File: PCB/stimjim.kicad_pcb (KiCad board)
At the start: 4 copper layers, 129 x 79.5 mm, 193 parts, among them J1 Conn_02x08_Odd_Even, J10 USB4105-GF-A, J11 BM03B-SRSS-TB, J2 Conn_Coaxial, J3 Conn_Coaxial, J4 10129383-910002ALF, J6 Screw_Terminal_01x02, J7 Conn_Coaxial, J8 Screw_Terminal_01x02, J9 Conn_Coaxial, SW2 PTS645VH58-2 LFS, SW3 TS04-66-50-BK-160-SMT, U10 AMP03, U11 INA826, U12 DG509ACWE, U13 CC3-0512DF-E, U14 ISO7760, U15 ISO7741, U151 AP2112K-3.3, U16 L78L05_SO8, U17 AD5752, U18 AD7321, U19 AD1582, U2 CC3-0512DF-E, U20 OPA197, U21 AMP03, U22 INA826, U23 DG509ACWE, U24 RP2354B, U25 W25Q128JVS, U3 ISO7760, U4 ISO7741, U5 L78L05_SO8, U6 AD5752, U7 AD7321, U8 AD1582, U9 OPA197, Y1 ABM8AIG-12.000MHZ-12-2Z-T3

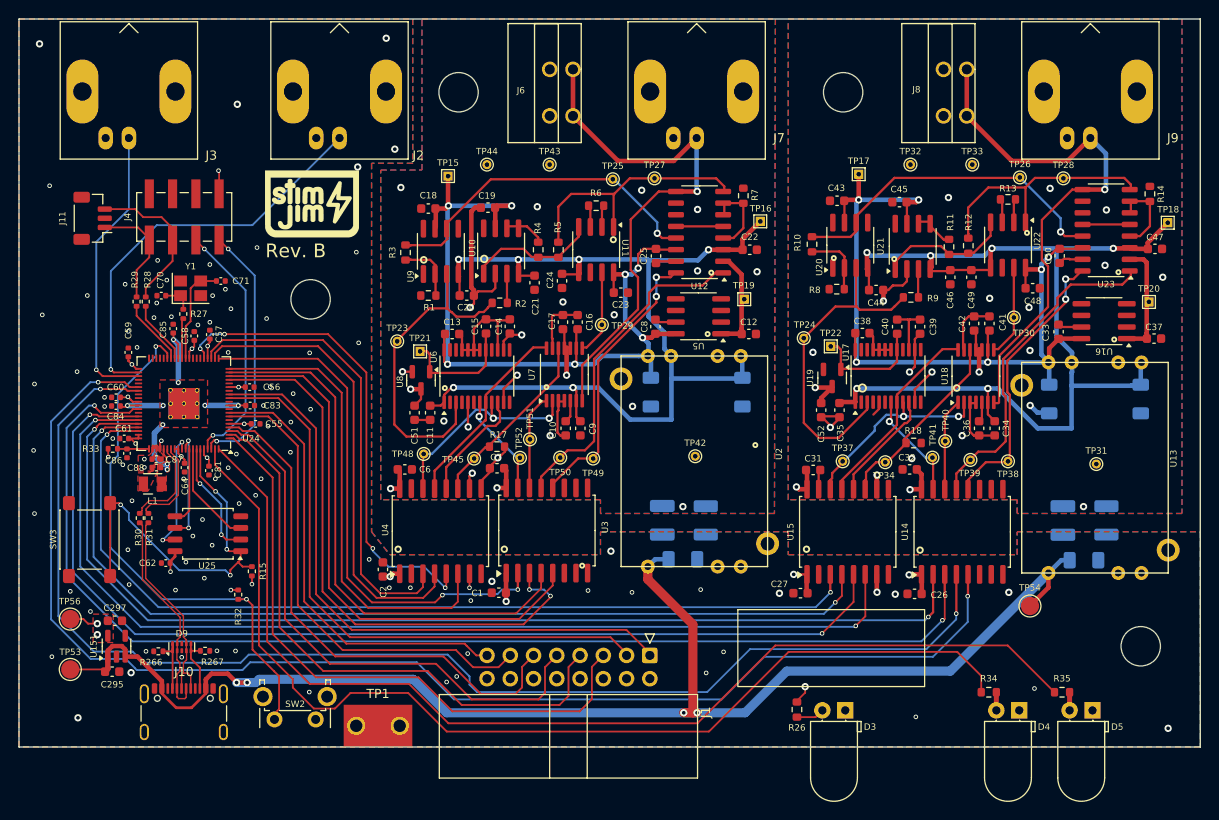
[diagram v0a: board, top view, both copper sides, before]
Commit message: Stimjim Rev. B candidate
- Sent to fab
- Lots of manufacturability changes
- BOM consolidation
- Repo layout changed a bit to remove redundant information. e.g.
  datasheet links are embedded in schematic. BOM information embedded in
  schematic. etc
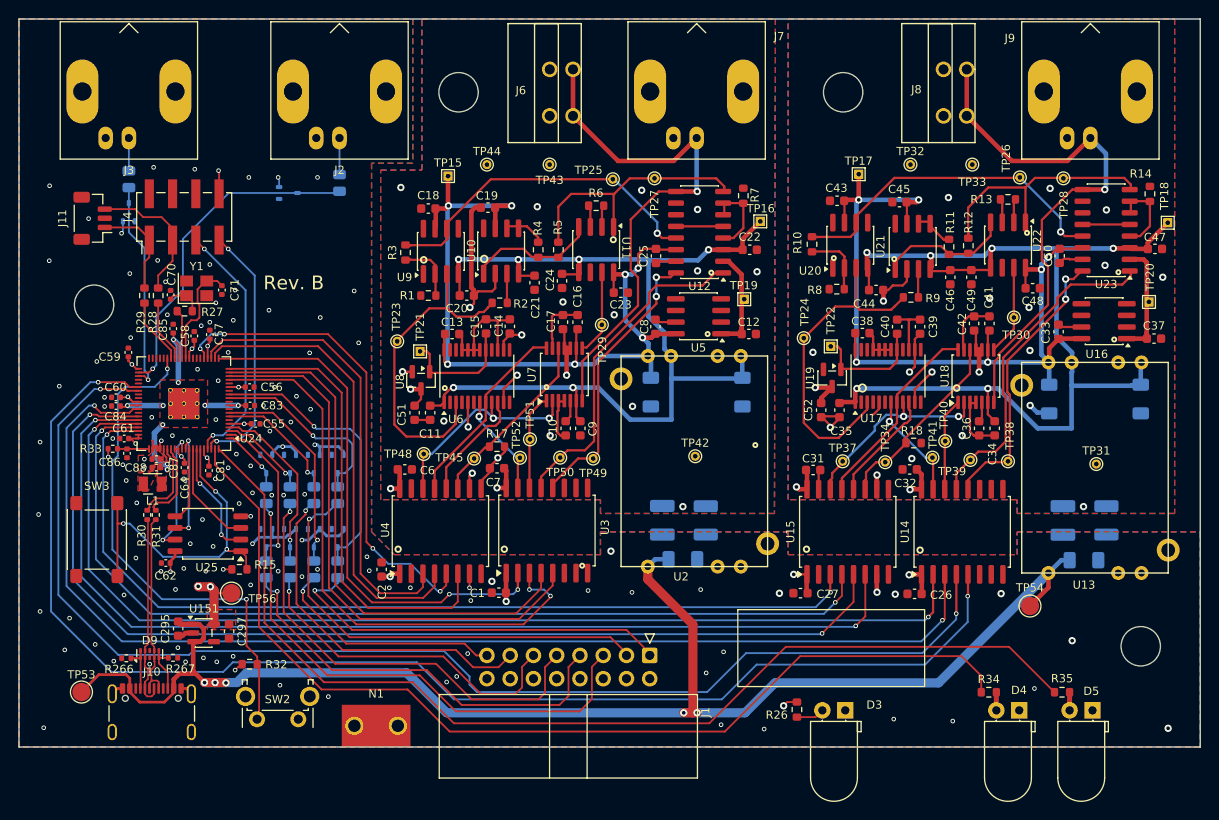
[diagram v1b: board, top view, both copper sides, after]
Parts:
- removed the G*** at (179.1, 108.4)
- removed the G*** at (178.9, 108.4)
- added D1: BAT54SW, Package_TO_SOT_SMD:SOT-323_SC-70, B.Cu at (176.4, 107.5)
- added D10: BAT54SW, Package_TO_SOT_SMD:SOT-323_SC-70, B.Cu at (179.2, 137.1)
- added D11: BAT54SW, Package_TO_SOT_SMD:SOT-323_SC-70, B.Cu at (176.6, 145.2)
- added D12: BAT54SW, Package_TO_SOT_SMD:SOT-323_SC-70, B.Cu at (176.6, 137.1)
- added D13: BAT54SW, Package_TO_SOT_SMD:SOT-323_SC-70, B.Cu at (174.0, 145.2)
- added D14: BAT54SW, Package_TO_SOT_SMD:SOT-323_SC-70, B.Cu at (174.0, 137.1)
- added D15: BAT54SW, Package_TO_SOT_SMD:SOT-323_SC-70, B.Cu at (181.8, 137.1)
- added D16: BAT54SW, Package_TO_SOT_SMD:SOT-323_SC-70, B.Cu at (181.8, 145.2)
- added D6: BAT54SW, Package_TO_SOT_SMD:SOT-323_SC-70, B.Cu at (159.0, 109.6)
- added D8: BAT54SW, Package_TO_SOT_SMD:SOT-323_SC-70, B.Cu at (179.2, 145.2)
- added G***: LOGO, LOGO, F.Cu at (178.2, 110.9)
- added R16: 270, Resistor_SMD:R_0805_2012Metric, B.Cu at (159.0, 106.0)
- added R21: 270, Resistor_SMD:R_0805_2012Metric, B.Cu at (179.2, 148.6)
- added R22: 270, Resistor_SMD:R_0805_2012Metric, B.Cu at (179.2, 140.5)
- added R23: 270, Resistor_SMD:R_0805_2012Metric, B.Cu at (176.6, 148.6)
- added R24: 270, Resistor_SMD:R_0805_2012Metric, B.Cu at (176.6, 140.5)
- added R25: 270, Resistor_SMD:R_0805_2012Metric, B.Cu at (174.0, 148.6)
- added R36: 270, Resistor_SMD:R_0805_2012Metric, B.Cu at (174.0, 140.5)
- added R37: 270, Resistor_SMD:R_0805_2012Metric, B.Cu at (181.8, 140.5)
- added R38: 270, Resistor_SMD:R_0805_2012Metric, B.Cu at (181.8, 148.6)
- added R39: 270, Resistor_SMD:R_0805_2012Metric, B.Cu at (182.0, 106.4)
- J1: value Conn_02x08_Odd_Even -> 302-R161
- J2, J3, J7, J9: value Conn_Coaxial -> 0731375003
- J6, J8: value Screw_Terminal_01x02 -> 1-2834016-2
- N1: renamed from TP1; value TestPoint -> SMTRA_M3-7-5ET
- R15, R27, R28, R29, R32: footprint Resistor_SMD:R_0402_1005Metric -> Resistor_SMD:R_0603_1608Metric
- R19, R20: value 1M -> 2.2M
- R33: value 33 -> 27
- U12, U23: value DG509ACWE -> DG409DYZ-T
- U16, U5: value L78L05_SO8 -> MC78L05ACDR2G
- moved H3 23.6 mm to (155.2, 119.7)
- moved TP56 17.8 mm to (170.2, 151.2), turned to 0 degrees
- moved C297 12.5 mm to (169.9, 155.4), turned to -90 degrees
- moved U151 9.62 mm to (167.2, 155.5), turned to 0 degrees
- moved C295 8.60 mm to (164.4, 155.1), turned to -90 degrees
- moved R32 7.70 mm to (172.2, 159.0), turned to 0 degrees
- moved D9 3.58 mm to (161.3, 157.9)
- moved R266 3.58 mm to (158.7, 158.3)
- moved R267 3.58 mm to (163.8, 158.3)
- moved J10 3.50 mm to (161.5, 165.3)
- moved TP53 2.75 mm to (153.8, 162.0)
- moved SW2 1.90 mm to (177.5, 165.0)
- moved R28 1.51 mm to (162.2, 118.7)
- moved R15 1.38 mm to (171.1, 148.6), turned to 0 degrees
- moved R29 1.08 mm to (160.7, 118.7)
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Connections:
- J1 pad 1: /GPIO0 -> /MCU/GPIO7_{P}
- J1 pad 11: /GPIO5 -> /MCU/GPIO2_{P}
- J1 pad 13: /GPIO6 -> /MCU/GPIO1_{P}
- J1 pad 15: /GPIO7 -> /MCU/GPIO0_{P}
- J1 pad 3: /GPIO1 -> /MCU/GPIO6_{P}
- J1 pad 5: /GPIO2 -> /MCU/GPIO5_{P}
- J1 pad 7: /GPIO3 -> /MCU/GPIO4_{P}
- J1 pad 9: /GPIO4 -> /MCU/GPIO3_{P}
- U24 pad 1: /GPIO2 -> /MCU/GPIO5
- U24 pad 12: /GPIO1 -> /MCU/GPIO6
- U24 pad 13: /GPIO0 -> /MCU/GPIO7
- U24 pad 2: /GPIO3 -> /MCU/GPIO4
- U24 pad 3: /GPIO4 -> /MCU/GPIO3
- U24 pad 4: /GPIO5 -> /MCU/GPIO2
- U24 pad 42: Net-(J2-In) -> /MCU/TRIG0
- U24 pad 43: Net-(J3-In) -> /MCU/TRIG1
- U24 pad 7: /GPIO6 -> /MCU/GPIO1
- U24 pad 8: /GPIO7 -> /MCU/GPIO0
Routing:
- net /GPIO0: track 68.3 -> 0.00 mm
- net /GPIO2: track 67.8 -> 0.00 mm
- net /GPIO1: track 65.7 -> 0.00 mm
- net /GPIO3: track 64.5 -> 0.00 mm
- net /GPIO4: track 61.0 -> 0.00 mm
- net /GPIO5: track 57.6 -> 0.00 mm
- net /MCU/GPIO5_{P}: track 0.00 -> 57.3 mm, vias 0 -> 1
- net /GPIO6: track 52.8 -> 0.00 mm
- net /MCU/GPIO6_{P}: track 0.00 -> 49.6 mm, vias 0 -> 1
- net /MCU/GPIO3_{P}: track 0.00 -> 49.6 mm, vias 0 -> 1
- net /GPIO7: track 49.2 -> 0.00 mm
- net /MCU/GPIO4_{P}: track 0.00 -> 46.2 mm, vias 0 -> 1
- net /MCU/GPIO7_{P}: track 0.00 -> 43.0 mm, vias 0 -> 1
- net Net-(J2-In): track 44.9 -> 3.99 mm, vias 1 -> 0
- net /MCU/GPIO1_{P}: track 0.00 -> 38.6 mm, vias 0 -> 1
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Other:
- board text added: "(e.g. JLC04161H-7628)"
- board text added: "0"
- board text added: "0 mm"
- board text added: "0.01 mm"
- board text added: "0.0152 mm"
- board text added: "0.02"
- board text added: "0.035 mm"
- board text added: "0.2104 mm"
- board text added: "1"
- board text added: "1.065 mm"
- board text added: "3.3"
- board text added: "4.5"
- board text added: "B.Cu"
- board text added: "B.Mask"
- board text added: "B.Paste"
- board text added: "B.Silkscreen"
- board text added: "Bottom Silk Screen"
- board text added: "Bottom Solder Mask"
- board text added: "Bottom Solder Paste"
- board text added: "Color"
- board text added: "Dielectric 1"
- board text added: "Dielectric 2"
- board text added: "Dielectric 3"
- board text added: "Epsilon R"
- board text added: "F.Cu"
- board text added: "F.Mask"
- board text added: "F.Paste"
- board text added: "F.Silkscreen"
- board text added: "FR4"
- board text added: "In1.Cu"
- board text added: "In2.Cu"
- board text added: "Layer Name"
- board text added: "Loss Tangent"
- board text added: "Material"
- board text added: "Not specified"
- board text added: "Thickness (mm)"
- board text added: "Top Silk Screen"
- board text added: "Top Solder Mask"
- board text added: "Top Solder Paste"
- board text added: "Type"
- board text added: "copper"
- board text added: "core"
- board text added: "prepreg"

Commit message: Rev C First Draft
- Fix and move LED footprints
- Move bar code sticker
- Add op-amp unity voltage follower to ADC input
- Remove screw terminals
- Made panel screw holes bigger both panels (3.2mm -> 3.7mm) for 3.4mm
  screws
- Create cutout for mounting rail on panels
- Delete the file with both back and front panels
- Update all footprints (except rp2354b so that its thermal vias pass DRC)
- Add component class and custom rule for USB-C footprint
- Indicate M3 screw in schematic + Add to BOM
- Improve adherence to ADC/DAC datasheets:
  - Move high speed signals out from under ADC (put MISO in +5V layer under ADC)
  - Add 10uF decoupling caps to ADC/DAC
- Change enclosure part number to black enclosure
- Add some more GND vias to isolated GND planes
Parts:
- removed J6, J8: 1-2834016-2, microstim:1-2834016-2 _TERM_BLK_2P_SIDE_ENT_2.54MM_PCB
- added C63: 0.1uF, Capacitor_SMD:C_0603_1608Metric, F.Cu at (244.8, 100.9)
- added C65: 0.1uF, Capacitor_SMD:C_0603_1608Metric, F.Cu at (201.8, 101.8)
- added C66: 0.1uF, Capacitor_SMD:C_0603_1608Metric, F.Cu at (254.5, 97.6)
- added C67: 0.1uF, Capacitor_SMD:C_0603_1608Metric, F.Cu at (211.5, 98.6)
- added C68: 10uF, Capacitor_SMD:C_0603_1608Metric, F.Cu at (239.1, 121.3)
- added C69: 10uF, Capacitor_SMD:C_0603_1608Metric, F.Cu at (192.1, 122.2)
- added C72: 10uF, Capacitor_SMD:C_0603_1608Metric, F.Cu at (235.6, 131.4)
- added C73: 10uF, Capacitor_SMD:C_0603_1608Metric, F.Cu at (190.8, 131.7)
- added C74: 10uF, Capacitor_SMD:C_0603_1608Metric, F.Cu at (253.8, 122.2)
- added C75: 10uF, Capacitor_SMD:C_0603_1608Metric, F.Cu at (209.3, 121.7)
- added C76: 10uF, Capacitor_SMD:C_0603_1608Metric, F.Cu at (254.8, 132.9)
- added C77: 10uF, Capacitor_SMD:C_0603_1608Metric, F.Cu at (209.6, 132.7)
- added U1: OPA197, Package_SO:SOIC-8_3.9x4.9mm_P1.27mm, F.Cu at (250.0, 99.0)
- added U26: OPA197, Package_SO:SOIC-8_3.9x4.9mm_P1.27mm, F.Cu at (207.0, 100.0)
- D3, D4, D5: footprint microstim:LED_D5.0mm_Horizontal_O1.27mm_Z3.0mm_pinSwapped -> open-ephys:LUMEX_SSF-LHXH100GD-01
- SW3: footprint Button_Switch_SMD:SW_SPST_PTS645Sx43SMTR92 -> open-ephys:SAMESKY_TS04-66-XX-BK-XXX-SMT-XX
- moved H5 56.9 mm to (180.1, 145.0), turned to 90 degrees
- moved R35 6.51 mm to (258.9, 155.8)
- moved R34 4.50 mm to (248.4, 161.8)
- moved TP33 3.49 mm to (248.0, 102.8)
- moved TP32 2.61 mm to (241.8, 104.2)
- moved D3 2.20 mm to (234.7, 161.8), turned to 180 degrees
- moved D4 2.20 mm to (253.7, 161.8), turned to 180 degrees
- moved D5 2.20 mm to (261.7, 161.8), turned to 180 degrees
- moved H4 2.06 mm to (270.0, 155.0)
- moved R26 1.77 mm to (230.3, 163.4), turned to 90 degrees
- moved C51 1.42 mm to (189.3, 130.4)
- moved TP43 1.14 mm to (204.2, 103.5)
- moved C52 1.12 mm to (234.2, 130.2)
- moved TP49 1.07 mm to (210.8, 136.4)
- moved C46 0.98 mm to (247.8, 117.1)
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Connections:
- U18 pad 7: /channel_0/CHANNEL_OUT -> Net-(U1--)
- U7 pad 7: /channel_1/CHANNEL_OUT -> Net-(U26--)
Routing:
- net Net-(U1--): track 0.00 -> 60.6 mm, vias 0 -> 2
- net Net-(U26--): track 0.00 -> 58.7 mm, vias 0 -> 2
- net /channel_0/-15V: track 112.8 -> 149.2 mm
- net /channel_1/-15V: track 108.6 -> 141.4 mm
- net /channel_1/CHANNEL_OUT: track 59.1 -> 27.6 mm
- net /channel_0/CHANNEL_OUT: track 58.9 -> 27.6 mm
- net /channel_0/+15V: track 90.1 -> 115.2 mm
- net /channel_1/+15V: track 92.0 -> 116.1 mm
- net /channel_0/GRND: track 44.2 -> 35.3 mm, vias 15 -> 34
- net /channel_1/GRND: track 56.4 -> 47.5 mm, vias 16 -> 36
- net VCC: track 86.2 -> 77.6 mm
- net Net-(D5-A): track 1.97 -> 6.28 mm
- net Net-(U24-GPIO2): track 111.0 -> 107.1 mm
- net Net-(U24-GPIO3): track 117.4 -> 113.8 mm
- net /channel_0/OE0_i: track 36.3 -> 39.3 mm
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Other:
- board text added: "Rev. C"
- board text removed: "Rev. B"
